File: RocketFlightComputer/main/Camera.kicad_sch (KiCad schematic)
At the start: 0 parts

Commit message: Camera and reserve
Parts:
- added JST4PIN2: S4B-PH-K-S_LF__SN_, Connector_JST:JST_GH_BM04B-GHS-TBT_1x04-1MP_P1.25mm_Vertical, symbol B3P-VH_LF__SN_:S4B-PH-K-S_LF__SN_
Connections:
- new net +7.5V: JST4PIN2.2
- new net Cam_RX: JST4PIN2.3
- new net Cam_TX: JST4PIN2.4
- new net GNDREF: JST4PIN2.1

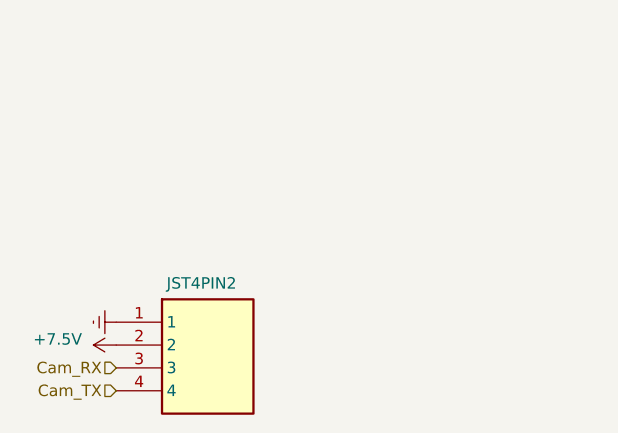
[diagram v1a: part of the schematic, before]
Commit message: CID documentation and started the PCB editor process
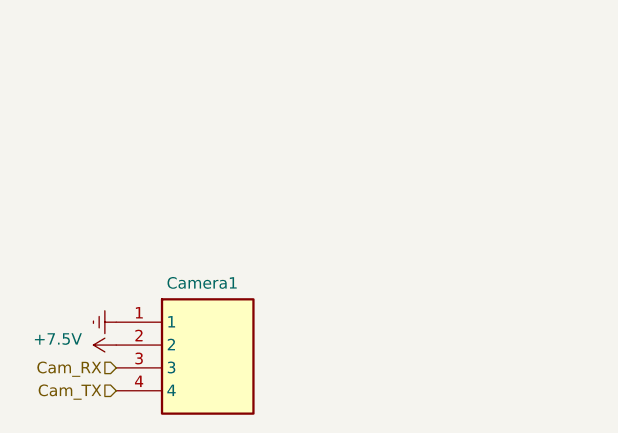
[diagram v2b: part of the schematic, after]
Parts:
- renumbered JST4PIN2 to Camera1
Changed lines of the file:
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@@
 		(on_board yes)
 		(dnp no)
-		(property "Reference" "JST4PIN2"
+		(property "Reference" "Camera1"
 			(at 130.048 85.852 0)
 			(effects
@@
 			(project "main"
 				(path "/27195d1d-92b2-40df-ada5-3b20841577e7/e516ca7f-4a7c-4d6f-878d-eb9fde5d9c52"
-					(reference "JST4PIN2")
+					(reference "Camera1")
 					(unit 1)
 				)

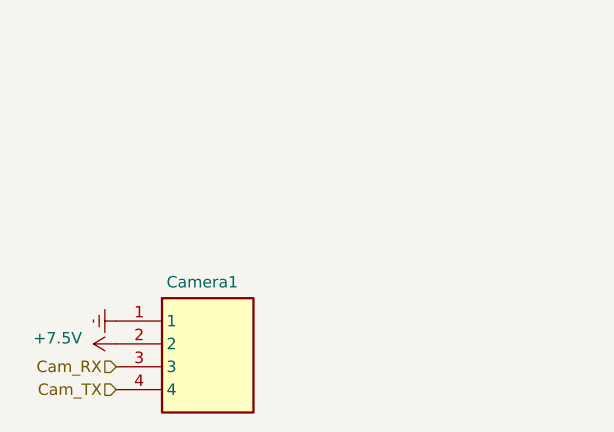
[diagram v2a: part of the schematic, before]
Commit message: Layout of PCB mostly done
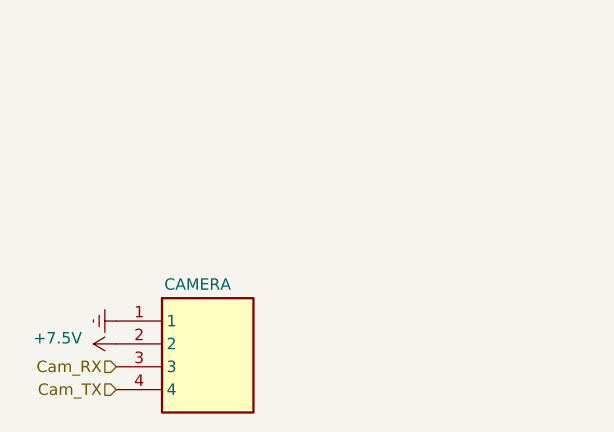
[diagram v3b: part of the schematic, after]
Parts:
- S4B-PH-K-S_LF__SN_2: renamed from Camera1; value S4B-PH-K-S_LF__SN_ -> CAMERA
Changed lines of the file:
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@@
 		(on_board yes)
 		(dnp no)
-		(property "Reference" "Camera1"
+		(property "Reference" "S4B-PH-K-S_LF__SN_2"
 			(at 130.048 85.852 0)
 			(effects
@@
 				)
 				(justify left)
+				(hide yes)
 			)
 		)
-		(property "Value" "S4B-PH-K-S_LF__SN_"
-			(at 140.97 95.2499 0)
+		(property "Value" "CAMERA"
+			(at 129.794 86.106 0)
 			(effects
 				(font
@@
 				)
 				(justify left)
-				(hide yes)
 			)
 		)
@@
 			(project "main"
 				(path "/27195d1d-92b2-40df-ada5-3b20841577e7/e516ca7f-4a7c-4d6f-878d-eb9fde5d9c52"
-					(reference "Camera1")
+					(reference "S4B-PH-K-S_LF__SN_2")
 					(unit 1)
 				)

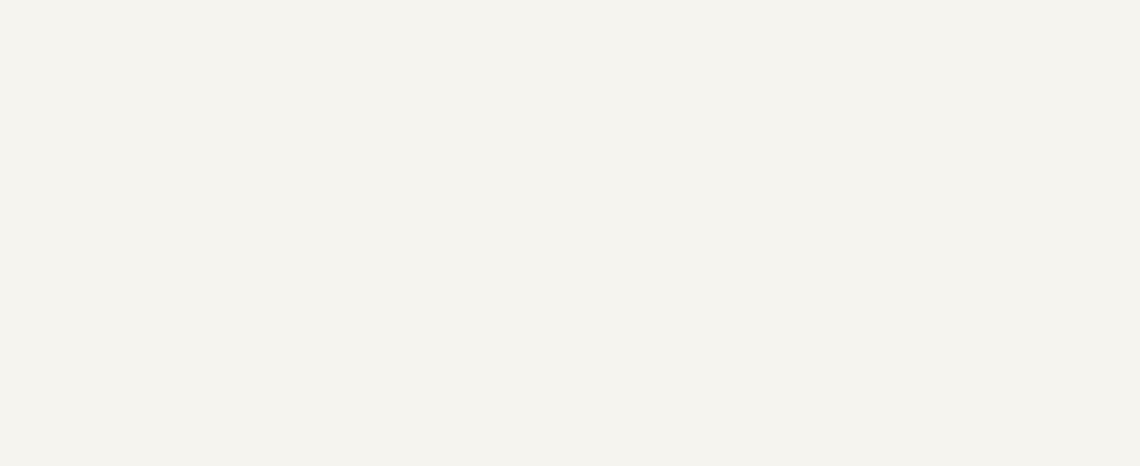
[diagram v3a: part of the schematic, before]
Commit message: Addition of teensy example and milestone on routing completed, missing a few components to connect
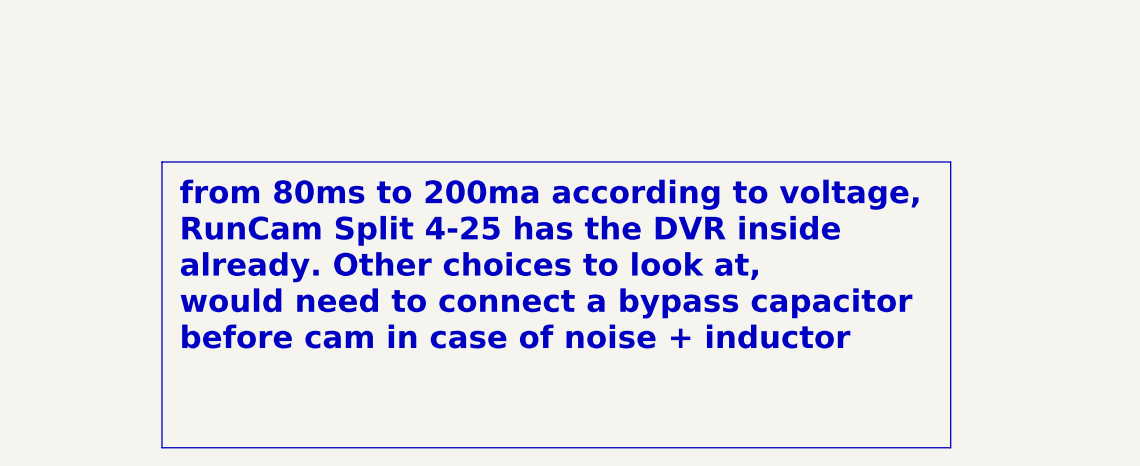
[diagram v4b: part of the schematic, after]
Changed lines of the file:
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@@
 	(generator_version "8.0")
 	(paper "A4")
+	(text_box "from 80ms to 200ma according to voltage, RunCam Split 4-25 has the DVR inside already. Other choices to look at, \nwould need to connect a bypass capacitor before cam in case of noise + inductor"
+		(exclude_from_sim no)
+		(at 177.165 121.92 0)
+		(size 87.63 31.75)
+		(stroke
+			(width 0)
+			(type default)
+		)
+		(fill
+			(type none)
+		)
+		(effects
+			(font
+				(size 2.5 2.5)
+				(thickness 0.254)
+				(bold yes)
+			)
+			(justify left top)
+		)
+	)
 	(text_box "Cameras use JST GH connectors"
 		(exclude_from_sim no)

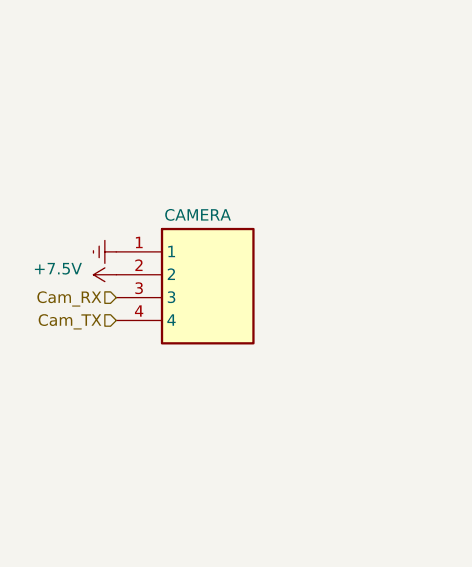
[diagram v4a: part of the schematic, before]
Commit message: First pass of verification and validation of pcb design
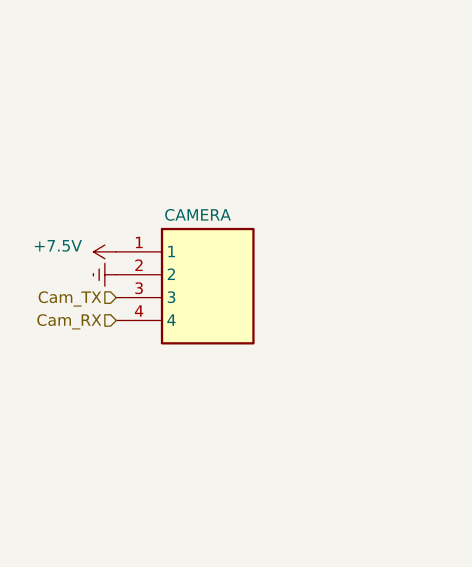
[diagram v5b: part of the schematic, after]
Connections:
- net +7.5V: now also S4B-PH-K-S_LF__SN_2.1; no longer S4B-PH-K-S_LF__SN_2.2
- net Cam_RX: now also S4B-PH-K-S_LF__SN_2.4; no longer S4B-PH-K-S_LF__SN_2.3
- net Cam_TX: now also S4B-PH-K-S_LF__SN_2.3; no longer S4B-PH-K-S_LF__SN_2.4
- net GNDREF: now also S4B-PH-K-S_LF__SN_2.2; no longer S4B-PH-K-S_LF__SN_2.1
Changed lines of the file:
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@@
 	(hierarchical_label "Cam_TX"
+		(shape input)
+		(at 124.46 95.25 180)
+		(fields_autoplaced yes)
+		(effects
+			(font
+				(size 1.27 1.27)
+			)
+			(justify right)
+		)
+	)
+	(hierarchical_label "Cam_RX"
 		(shape input)
 		(at 124.46 97.79 180)
@@
 		)
 	)
-	(hierarchical_label "Cam_RX"
-		(shape input)
-		(at 124.46 95.25 180)
-		(fields_autoplaced yes)
-		(effects
-			(font
-				(size 1.27 1.27)
-			)
-			(justify right)
-		)
-	)
 	(symbol
 		(lib_id "power:+7.5V")
-		(at 124.46 92.71 90)
+		(at 124.46 90.17 90)
 		(unit 1)
 		(exclude_from_sim no)
@@
 		(dnp no)
 		(property "Reference" "#PWR088"
-			(at 128.27 92.71 0)
+			(at 128.27 90.17 0)
 			(effects
 				(font
@@
 		)
 		(property "Value" "+7.5V"
-			(at 120.65 92.075 90)
+			(at 120.65 89.535 90)
 			(effects
 				(font
@@
 		)
 		(property "Footprint" ""
-			(at 124.46 92.71 0)
+			(at 124.46 90.17 0)
 			(effects
 				(font
@@
 		)
 		(property "Datasheet" ""
-			(at 124.46 92.71 0)
+			(at 124.46 90.17 0)
 			(effects
 				(font
@@
 		)
 		(property "Description" ""
-			(at 124.46 92.71 0)
+			(at 124.46 90.17 0)
 			(effects
 				(font
@@
 	(symbol
 		(lib_id "power:GNDREF")
-		(at 124.46 90.17 270)
+		(at 124.46 92.71 270)
 		(unit 1)
 		(exclude_from_sim no)
@@
 		(fields_autoplaced yes)
 		(property "Reference" "#PWR090"
-			(at 118.11 90.17 0)
+			(at 118.11 92.71 0)
 			(effects
 				(font
@@
 		)
 		(property "Value" "GNDREF"
-			(at 120.65 89.535 90)
+			(at 120.65 92.075 90)
 			(effects
 				(font
@@
 		)
 		(property "Footprint" ""
-			(at 124.46 90.17 0)
+			(at 124.46 92.71 0)
 			(effects
 				(font
@@
 		)
 		(property "Datasheet" ""
-			(at 124.46 90.17 0)
+			(at 124.46 92.71 0)
 			(effects
 				(font
@@
 		)
 		(property "Description" ""
-			(at 124.46 90.17 0)
-			(effects
-				(font
+			(at 124.46 92.71 0)
+			(effects
+				(font

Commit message: Addition of all components in BOM, metal mounting plates, need to check psram if its ok for signals to pass under, all components need a double check
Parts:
- S4B-PH-K-S_LF__SN_2: LCSC (none) -> C161692; Mouser Part Number N/A -> 306-BM04BGHSTBTLFSNN
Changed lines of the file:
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@@
 		(on_board yes)
 		(dnp no)
-		(property "Reference" "#PWR088"
+		(property "Reference" "#PWR0143"
 			(at 128.27 90.17 0)
 			(effects
@@
 			(project "main"
 				(path "/27195d1d-92b2-40df-ada5-3b20841577e7/e516ca7f-4a7c-4d6f-878d-eb9fde5d9c52"
-					(reference "#PWR088")
+					(reference "#PWR0143")
 					(unit 1)
 				)
@@
 			)
 		)
-		(property "Mouser Part Number" "N/A"
+		(property "Mouser Part Number" "306-BM04BGHSTBTLFSNN"
 			(at 140.97 585.09 0)
 			(effects
@@
 				)
 				(justify left top)
+				(hide yes)
+			)
+		)
+		(property "LCSC" "C161692"
+			(at 124.46 90.17 0)
+			(effects
+				(font
+					(size 1.27 1.27)
+				)
 				(hide yes)
 			)
@@
 		(dnp no)
 		(fields_autoplaced yes)
-		(property "Reference" "#PWR090"
+		(property "Reference" "#PWR0144"
 			(at 118.11 92.71 0)
 			(effects
@@
 			(project "main"
 				(path "/27195d1d-92b2-40df-ada5-3b20841577e7/e516ca7f-4a7c-4d6f-878d-eb9fde5d9c52"
-					(reference "#PWR090")
+					(reference "#PWR0144")
 					(unit 1)
 				)
